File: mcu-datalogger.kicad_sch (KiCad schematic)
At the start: 25 parts, among them U1 24LC1025, U2 24LC1025, U3 ATMEGA328-AU, U4 DS1337S+T&R, Y1 Crystal, Y2 Crystal

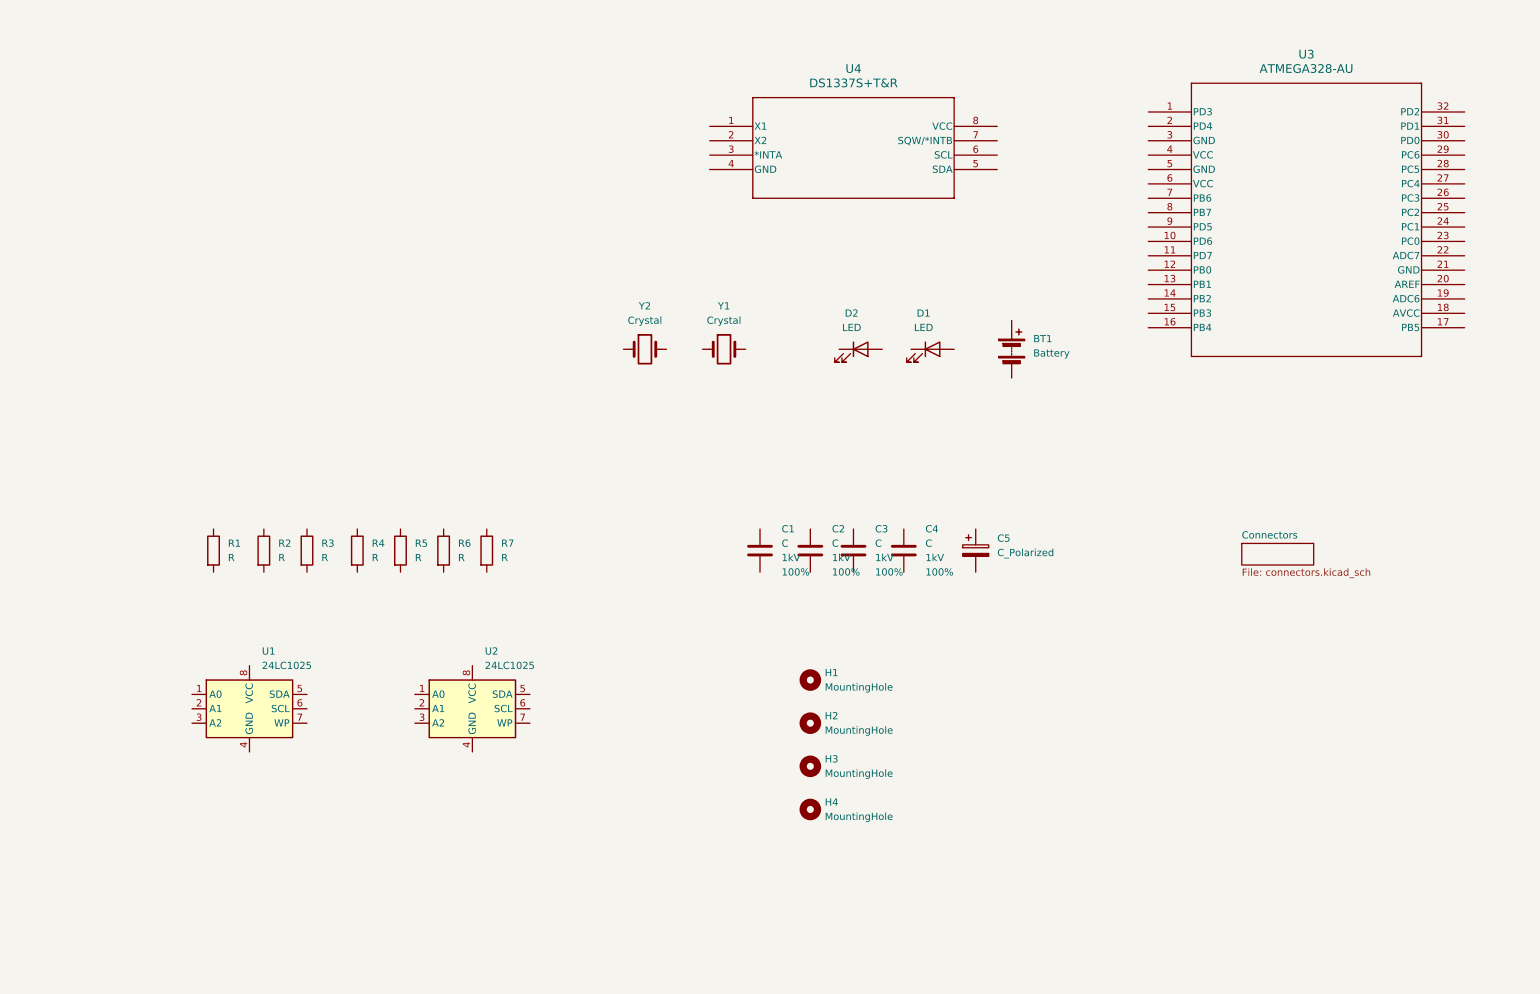
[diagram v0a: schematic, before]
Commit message: Rough arrange symbols
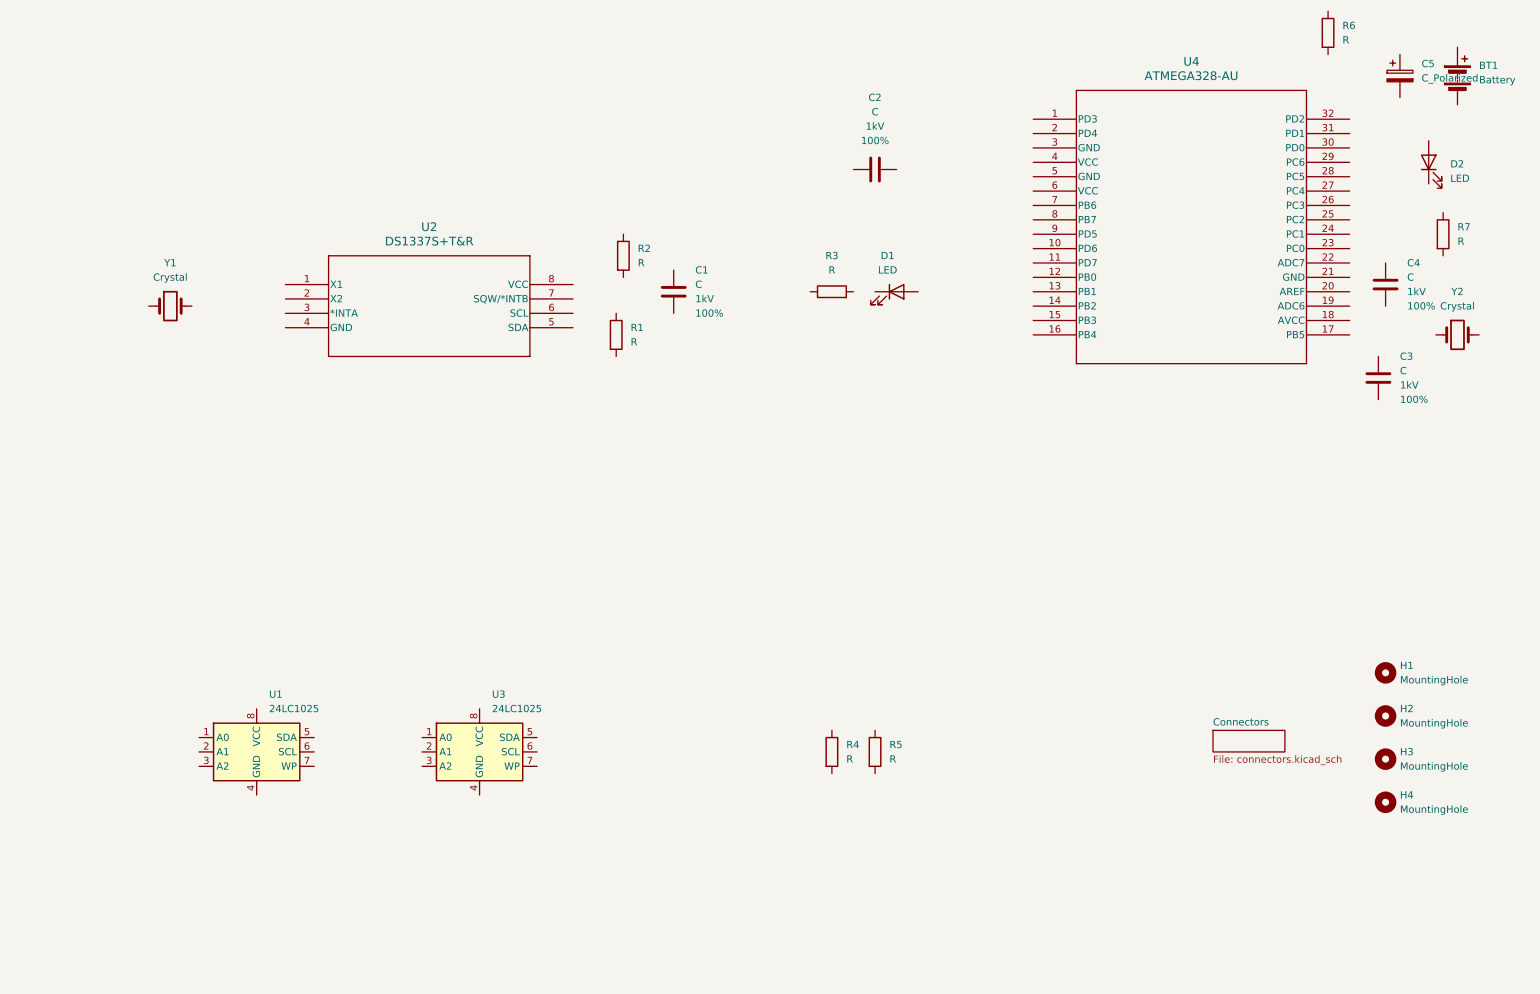
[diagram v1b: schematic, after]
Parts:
- renumbered C4 to C2, C2 to C3, C3 to C4, R4 to R1, R5 to R2, R6 to R3, R2 to R4, R3 to R5, R1 to R6, U4 to U2, U2 to U3, U3 to U4, Y2 to Y1, Y1 to Y2
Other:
- moved on the sheet: BT1, C1, C2, C3, C4, C5, D1, D2, H1, H2, H3, H4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

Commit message: Assign values to components.
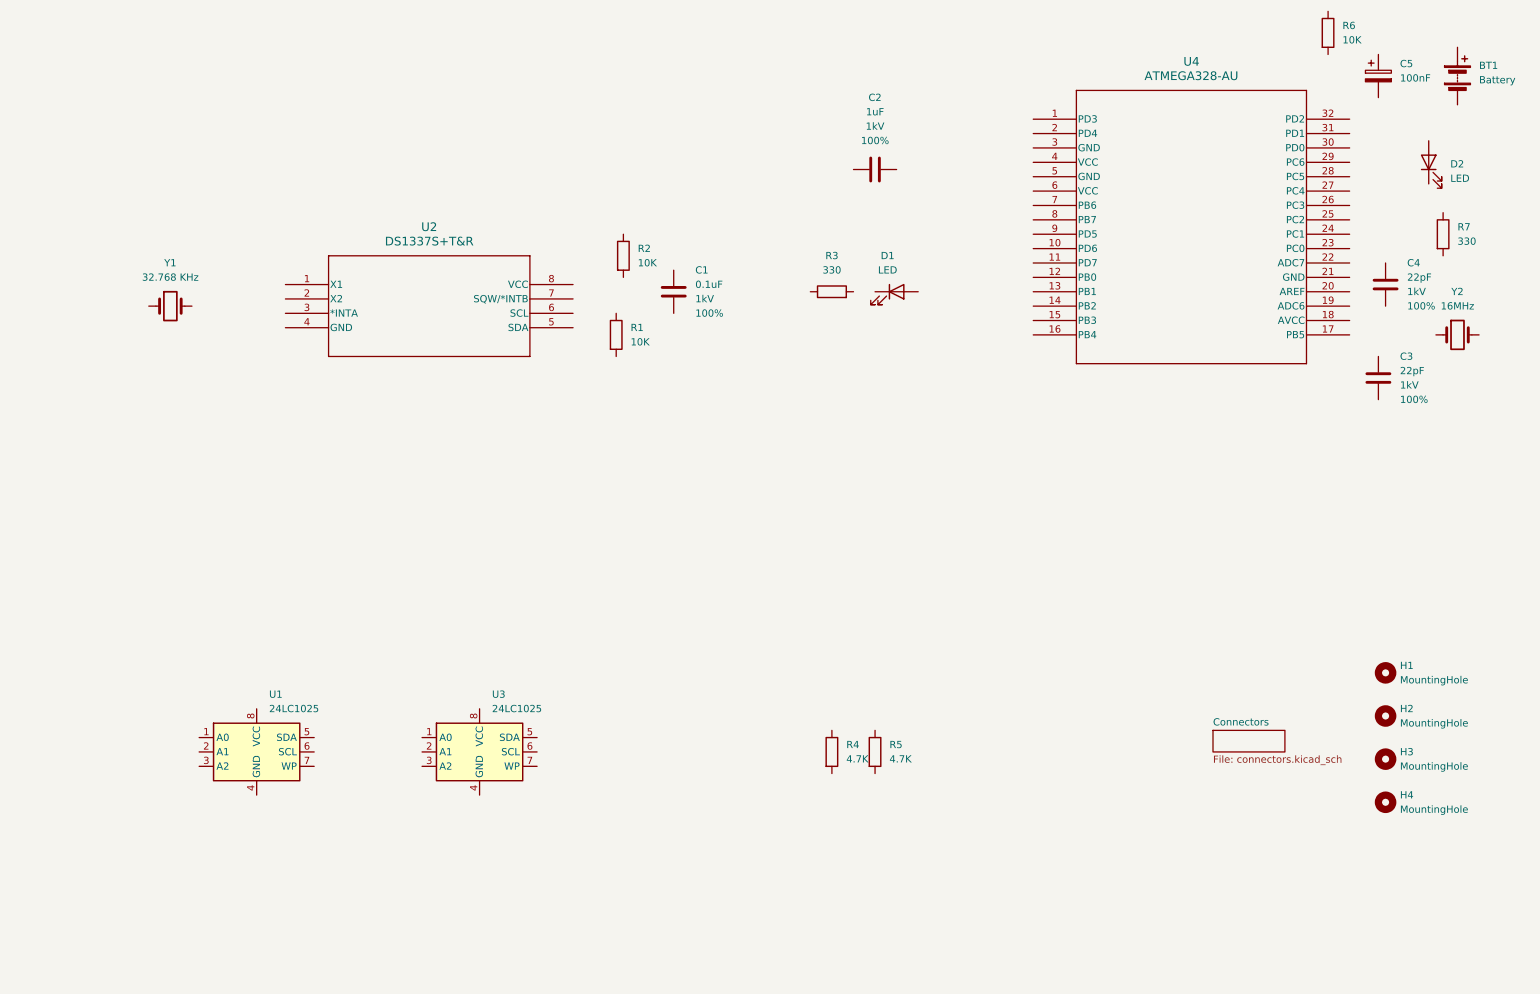
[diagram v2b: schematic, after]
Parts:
- C1: value C -> 0.1uF
- C2: value C -> 1uF
- C3, C4: value C -> 22pF
- C5: value C_Polarized -> 100nF
- R1, R2, R6: value R -> 10K
- R3, R7: value R -> 330
- R4, R5: value R -> 4.7K
- Y1: value Crystal -> 32.768 KHz
- Y2: value Crystal -> 16MHz
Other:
- moved on the sheet: C5
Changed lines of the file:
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@@
 			)
 		)
-		(property "Value" "Crystal"
+		(property "Value" "16MHz"
 			(at 273.05 68.58 0)
 			(effects
@@
 			)
 		)
+		(property "Purpose" ""
+			(at 273.05 73.66 0)
+			(effects
+				(font
+					(size 1.27 1.27)
+				)
+				(hide yes)
+			)
+		)
 		(pin "2"
 		)
@@
 			)
 		)
-		(property "Value" "R"
+		(property "Value" "10K"
 			(at 252.73 21.5899 0)
 			(effects
@@
 			)
 		)
+		(property "Purpose" ""
+			(at 250.19 20.32 0)
+			(effects
+				(font
+					(size 1.27 1.27)
+				)
+				(hide yes)
+			)
+		)
 		(pin "1"
 		)
@@
 			)
 		)
-		(property "Value" "R"
+		(property "Value" "10K"
 			(at 128.27 60.9599 0)
 			(effects
@@
 			)
 		)
+		(property "Purpose" ""
+			(at 125.73 59.69 0)
+			(effects
+				(font
+					(size 1.27 1.27)
+				)
+				(hide yes)
+			)
+		)
 		(pin "1"
 		)
@@
 			)
 		)
-		(property "Value" "Crystal"
+		(property "Value" "32.768 KHz"
 			(at 45.72 63.5 0)
 			(effects
@@
 			)
 		)
+		(property "Purpose" ""
+			(at 45.72 68.58 0)
+			(effects
+				(font
+					(size 1.27 1.27)
+				)
+				(hide yes)
+			)
+		)
 		(pin "2"
 		)
@@
 			)
 		)
-		(property "Value" "R"
+		(property "Value" "10K"
 			(at 127 74.9299 0)
 			(effects
@@
 			)
 		)
+		(property "Purpose" ""
+			(at 124.46 73.66 0)
+			(effects
+				(font
+					(size 1.27 1.27)
+				)
+				(hide yes)
+			)
+		)
 		(pin "1"
 		)
@@
 			)
 		)
-		(property "Value" "C"
+		(property "Value" "0.1uF"
 			(at 138.43 64.7699 0)
 			(effects
@@
 			)
 		)
+		(property "Purpose" ""
+			(at 134.62 66.04 0)
+			(effects
+				(font
+					(size 1.27 1.27)
+				)
+				(hide yes)
+			)
+		)
 		(pin "2"
 		)
@@
 			)
 		)
-		(property "Value" "R"
+		(property "Value" "4.7K"
 			(at 172.72 148.5899 0)
 			(effects
@@
 			)
 		)
+		(property "Purpose" ""
+			(at 170.18 147.32 0)
+			(effects
+				(font
+					(size 1.27 1.27)
+				)
+				(hide yes)
+			)
+		)
 		(pin "1"
 		)
@@
 			)
 		)
-		(property "Value" "C"
+		(property "Value" "22pF"
 			(at 262.89 80.0099 0)
 			(effects
@@
 			)
 		)
+		(property "Purpose" ""
+			(at 259.08 81.28 0)
+			(effects
+				(font
+					(size 1.27 1.27)
+				)
+				(hide yes)
+			)
+		)
 		(pin "2"
 		)
@@
 			)
 		)
-		(property "Value" "R"
+		(property "Value" "330"
 			(at 162.56 62.23 90)
 			(effects
@@
 			)
 		)
+		(property "Purpose" ""
+			(at 162.56 66.04 0)
+			(effects
+				(font
+					(size 1.27 1.27)
+				)
+				(hide yes)
+			)
+		)
 		(pin "1"
 		)
@@
 			)
 		)
-		(property "Value" "C"
+		(property "Value" "22pF"
 			(at 264.16 63.4999 0)
 			(effects
@@
 			)
 		)
+		(property "Purpose" ""
+			(at 260.35 64.77 0)
+			(effects
+				(font
+					(size 1.27 1.27)
+				)
+				(hide yes)
+			)
+		)
 		(pin "2"
 		)
@@
 	(symbol
 		(lib_id "Device:C_Polarized")
-		(at 262.89 27.94 0)
+		(at 259.08 27.94 0)
 		(unit 1)
 		(exclude_from_sim no)
@@
 		(fields_autoplaced yes)
 		(property "Reference" "C5"
-			(at 266.7 25.7809 0)
-			(effects
-				(font
-					(size 1.27 1.27)
-				)
-				(justify left)
-			)
-		)
-		(property "Value" "C_Polarized"
-			(at 266.7 28.3209 0)
+			(at 262.89 25.7809 0)
+			(effects
+				(font
+					(size 1.27 1.27)
+				)
+				(justify left)
+			)
+		)
+		(property "Value" "100nF"
+			(at 262.89 28.3209 0)
 			(effects
 				(font
@@
 		)
 		(property "Footprint" ""
-			(at 263.8552 31.75 0)
+			(at 260.0452 31.75 0)
 			(effects
 				(font
@@
 		)
 		(property "Datasheet" "~"
-			(at 262.89 27.94 0)
+			(at 259.08 27.94 0)
 			(effects
 				(font
@@
 		)
 		(property "Description" "Polarized capacitor"
-			(at 262.89 27.94 0)
+			(at 259.08 27.94 0)
+			(effects
+				(font
+					(size 1.27 1.27)
+				)
+				(hide yes)
+			)
+		)
+		(property "Purpose" ""
+			(at 259.08 27.94 0)
 			(effects
 				(font
@@
 			)
 		)
-		(property "Value" "R"
+		(property "Value" "4.7K"
 			(at 165.1 148.5899 0)
 			(effects
@@
 			)
 		)
+		(property "Purpose" ""
+			(at 162.56 147.32 0)
+			(effects
+				(font
+					(size 1.27 1.27)
+				)
+				(hide yes)
+			)
+		)
 		(pin "1"
 		)
@@
 			)
 		)
-		(property "Value" "C"
+		(property "Value" "1uF"
 			(at 170.18 34.29 90)
 			(effects
@@
 			)
 		)
+		(property "Purpose" ""
+			(at 170.18 44.45 0)
+			(effects
+				(font
+					(size 1.27 1.27)
+				)
+				(hide yes)
+			)
+		)
 		(pin "2"
 		)
@@
 			)
 		)
-		(property "Value" "R"
+		(property "Value" "330"
 			(at 273.05 57.1499 0)
 			(effects
@@
 			(at 270.51 55.88 0)
 			(effects
+				(font
+					(size 1.27 1.27)
+				)
+				(hide yes)
+			)
+		)
+		(property "Purpose" ""
+			(at 270.51 55.88 0)
+			(effects

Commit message: Associate footprints.
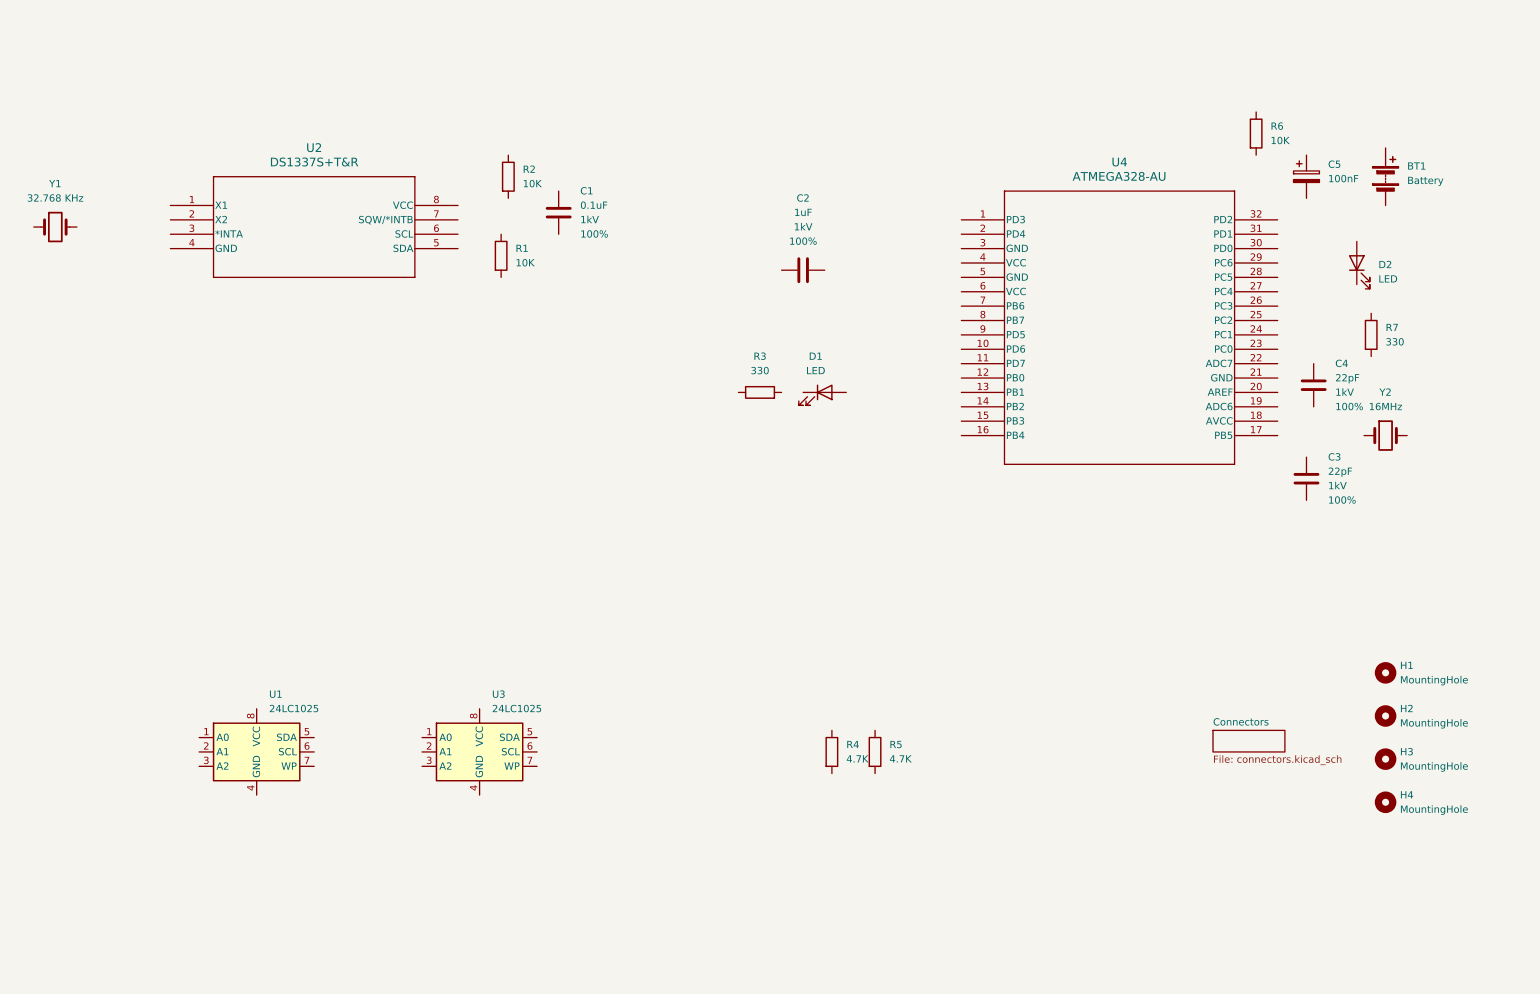
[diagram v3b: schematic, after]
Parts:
- BT1: footprint (none) -> Connector_PinHeader_2.54mm:PinHeader_1x02_P2.54mm_Vertical
- C1, C2, C3, C4: footprint SparkFun-Capacitor:C_0603_1608Metric -> Capacitor_SMD:C_0805_2012Metric
- C5: footprint (none) -> Capacitor_SMD:C_0805_2012Metric
- D1, D2: footprint SparkFun-LED:LED_0603_1608Metric -> LED_SMD:LED_0805_2012Metric
- H1, H2, H3, H4: footprint (none) -> MountingHole:MountingHole_2.1mm
- R1, R2, R3, R4, R5, R6, R7: footprint (none) -> Resistor_SMD:R_0805_2012Metric
- U1, U3: footprint (none) -> Package_SO:SOIC-8_5.23x5.23mm_P1.27mm
- U2: footprint 21-0041B_8_MXM -> footprints:DS1337S
- U4: footprint 32A_ATM -> footprints:ATMEGA328-AU
- Y1, Y2: footprint (none) -> Crystal:Crystal_SMD_5032-2Pin_5.0x3.2mm_HandSoldering
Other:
- moved on the sheet: BT1, C1, C2, C3, C4, C5, D1, D2, R1, R2, R3, R6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

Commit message: Wire main sheet
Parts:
- C2: value 1uF -> 0.1
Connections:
- net at Y2.1: now also C3.2, U4.8 (PB7)
- net at Y2.2: now also C4.2, U4.7 (PB6)
- net RESET: now reaches R6.1
- net RESET: now also U4.29 (PC6)
- net Vcc: now reaches R6.2
- net Vcc: now also C1.1, R1.1, R2.1, R4.1, R5.1, U1.1 (A0), U1.2 (A1), U1.3 (A2), U1.8 (VCC), U2.8 (VCC), U3.1 (A0), U3.3 (A2), U3.8 (VCC)
- net at R2.2: now also U2.7 (SQW/*INTB)
- net D3: now reaches U4.1 (PD3)
- net D6: now reaches U4.10 (PD6)
- net D7: now reaches U4.11 (PD7)
- net D8: now reaches U4.12 (PB0)
- net MOSI: now reaches U4.15 (PB3)
- net MISO: now reaches U4.16 (PB4)
- net at U4.17 (PB5): now also D1.2 (A)
- net AVCC: now reaches U4.18 (AVCC)
- net AVCC: now also BT1.1 (+), C5.1, D2.2 (A), U4.4 (VCC)
- net D4: now reaches U4.2 (PD4)
- net at U4.20 (AREF): now also C2.1
- net GND: now reaches U4.21 (GND)
- net GND: now also BT1.2 (-), C1.2, C2.2, C3.1, C4.1, C5.2, R3.1, R7.2, U1.4 (GND), U1.7 (WP), U2.4 (GND), U3.2 (A1), U3.4 (GND), U3.7 (WP), U4.3 (GND), U4.5 (GND)
- net SDA: now reaches U4.27 (PC4)
- net SDA: now also R5.2, U1.5 (SDA), U2.5 (SDA), U3.5 (SDA)
- net SCK: now reaches U4.28 (PC5)
- net SCK: now also R4.2, U1.6 (SCL), U2.6 (SCL), U3.6 (SCL)
- net RX: now reaches U4.30 (PD0)
- net TX: now reaches U4.31 (PD1)
- net D2: now reaches U4.32 (PD2)
- net D5: now reaches U4.9 (PD5)
- net at Y1.1: now also U2.2 (X2)
- net at Y1.2: now also U2.1 (X1)
- net at D2.1 (K): now also R7.1
- net at R1.2: now also U2.3 (*INTA)
- net at R3.2: now also D1.1 (K)
- no-connect marks 0 -> 9
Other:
- moved on the sheet: BT1, C1, C2, C3, C4, C5, D1, D2, R1, R2, R3, R4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
